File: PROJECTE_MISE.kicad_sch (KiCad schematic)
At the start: 46 parts, among them IC1 MSP430FR2355TPT, J1 conn_DFrobot, J10 SDA_{TP}, J11 SCL_{TP}, J12 SCL_{TP-GND}, J13 SPI_{TP-MISO}, J14 SPI_{TP-SS}, J15 SPI_{TP-SCLK}, J16 SPI_{TP-MOSI}, J17 SPI_{TP-GND}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

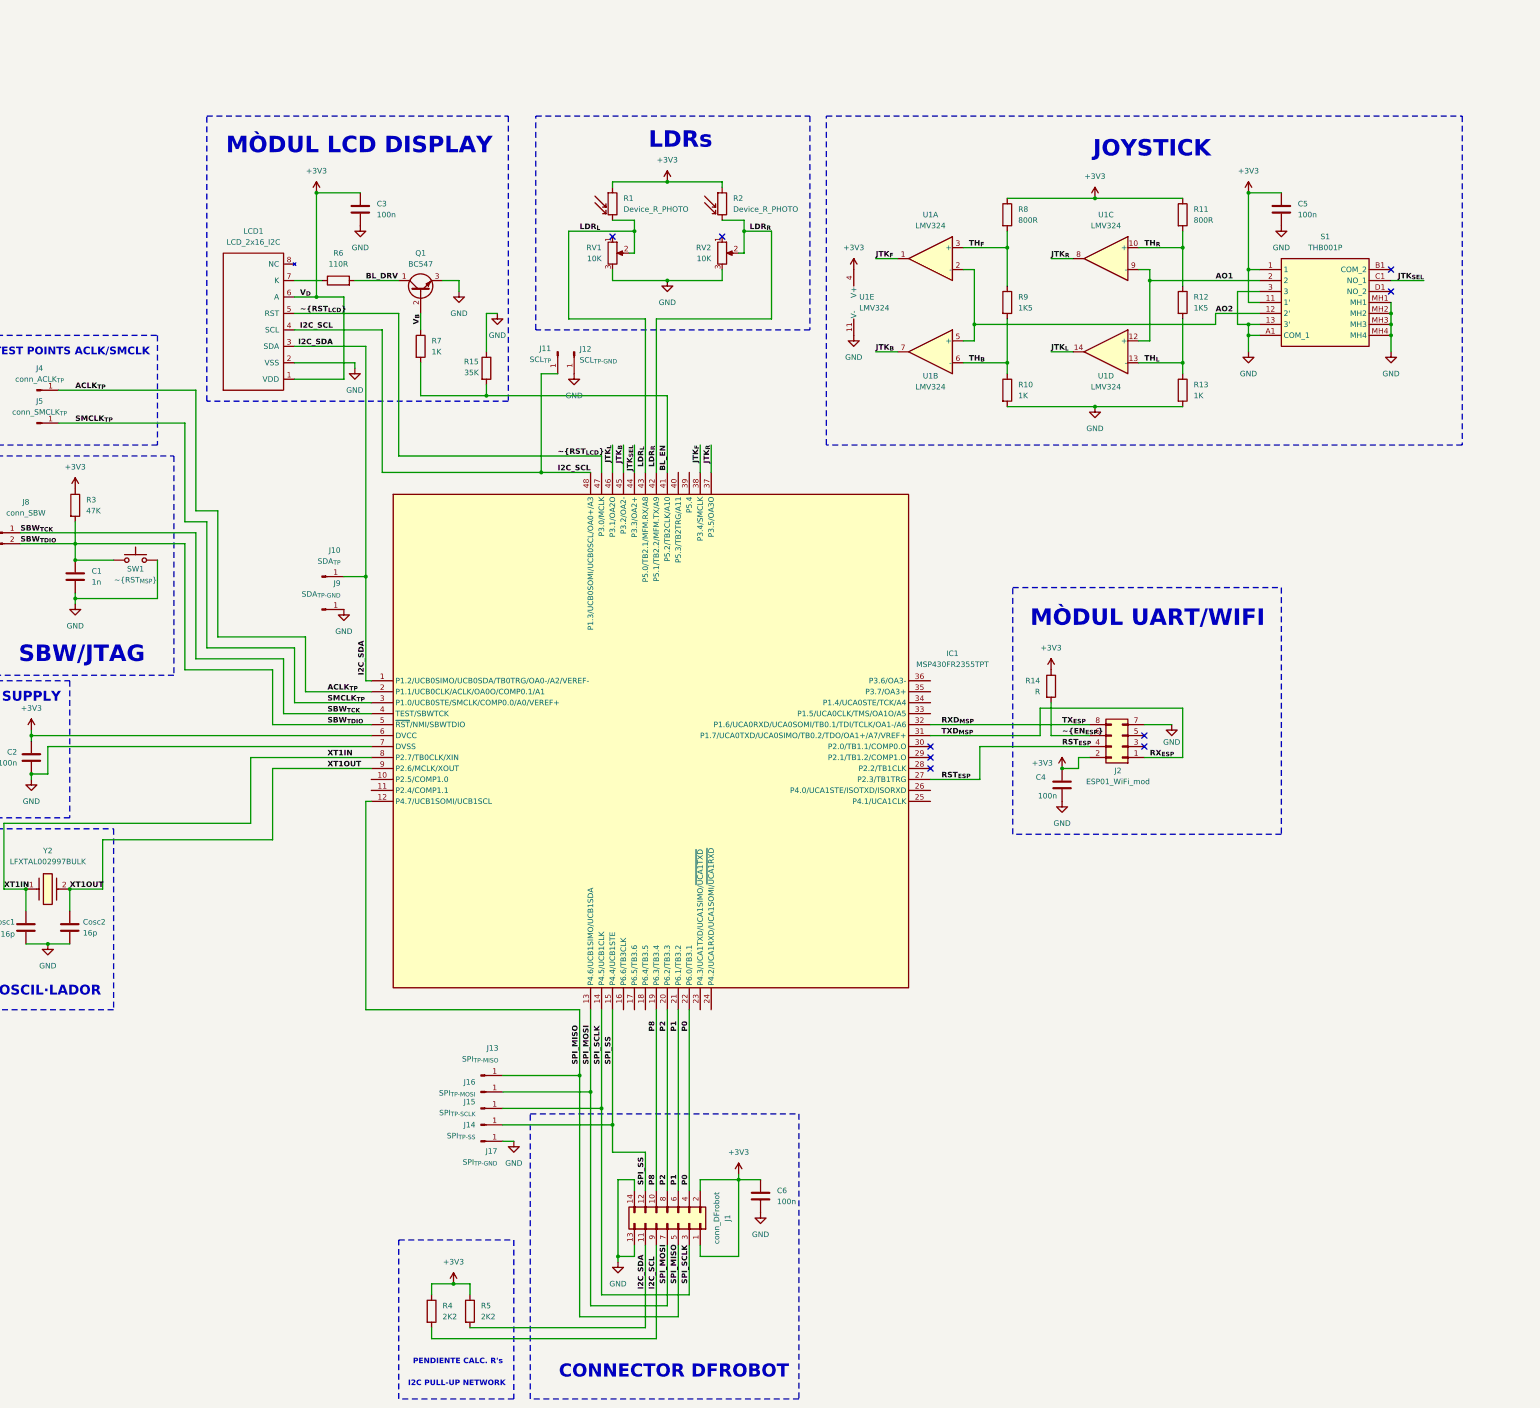
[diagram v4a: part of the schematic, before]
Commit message: placement i canvi esqu.
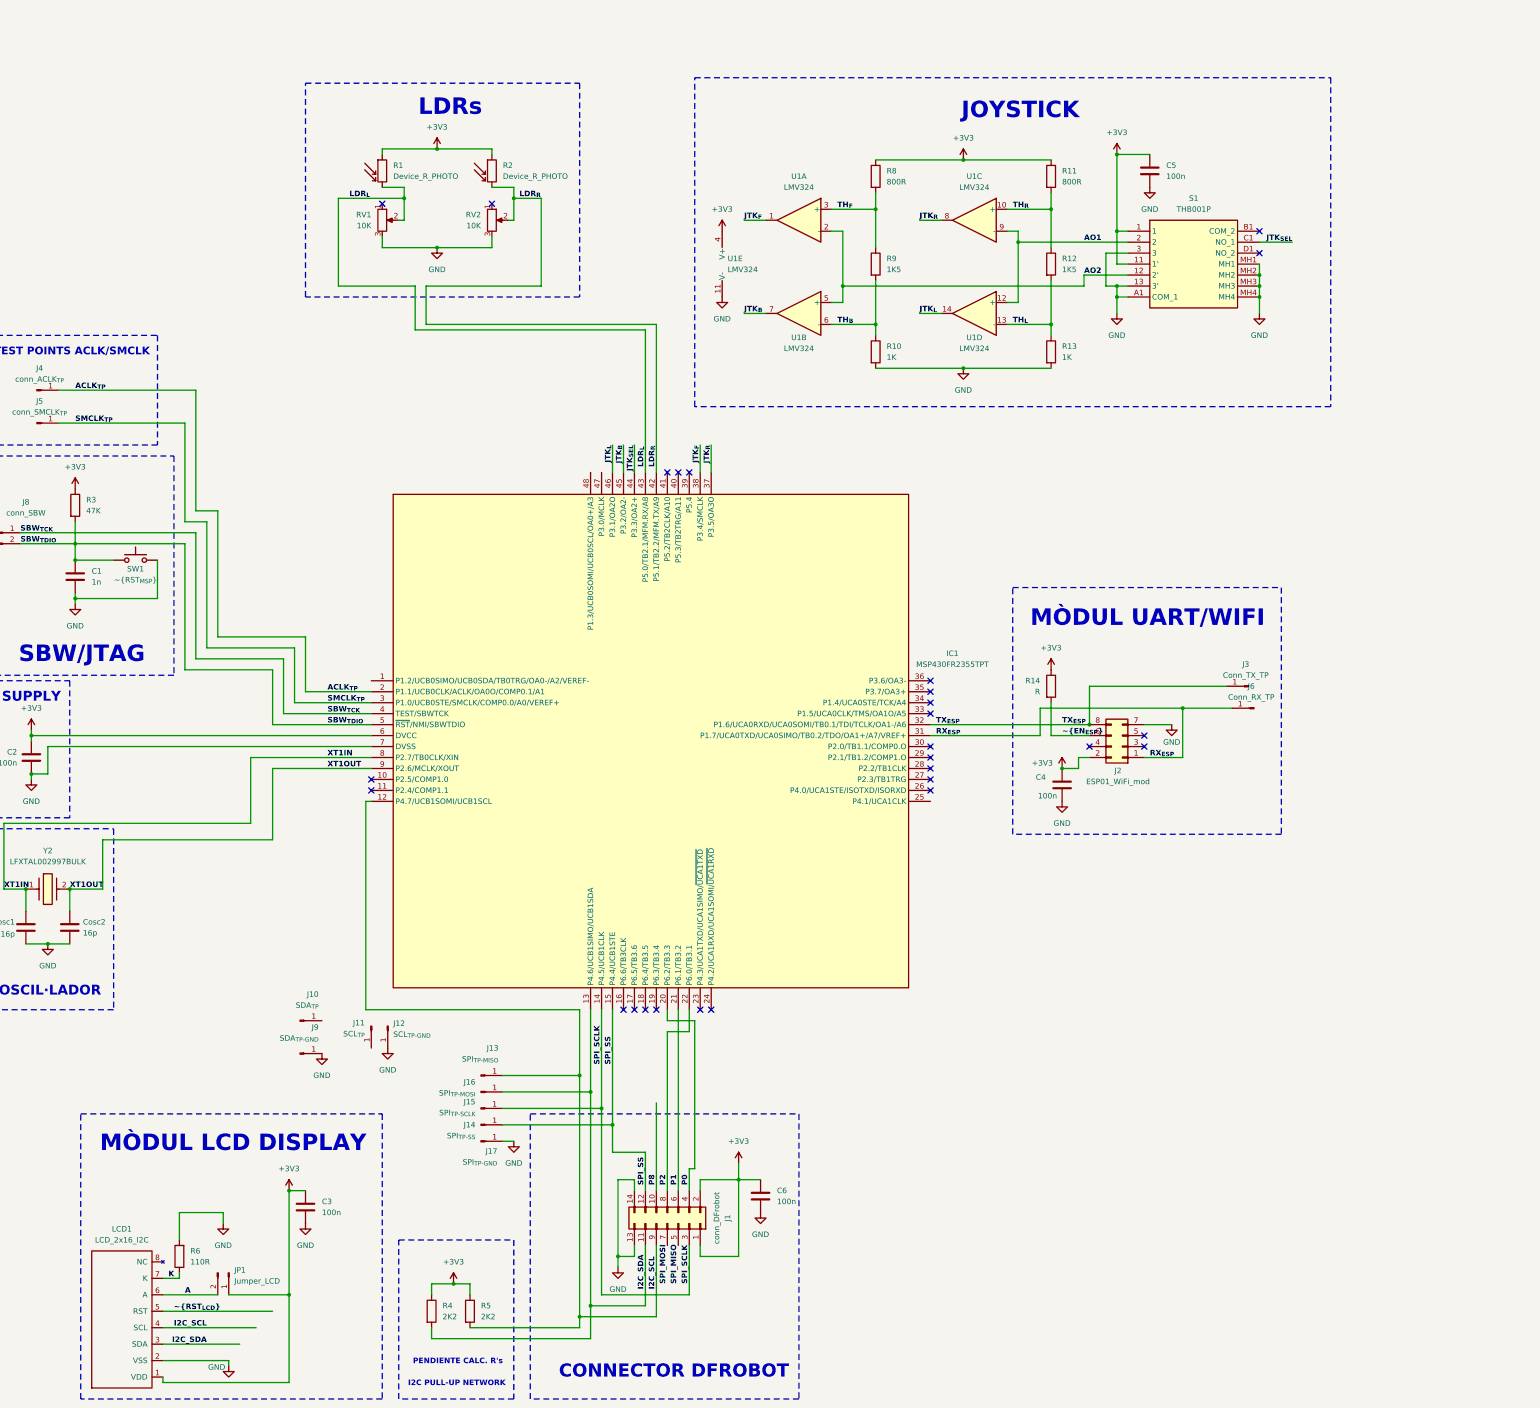
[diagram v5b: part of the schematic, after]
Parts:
- removed Q1: BC547, Package_TO_SOT_THT:TO-92_Inline, symbol Transistor_BJT:BC547
- removed R15: 35K, Resistor_SMD:R_0805_2012Metric, symbol Device:R
- removed R7: 1K, Resistor_SMD:R_0805_2012Metric, symbol Device:R
- added J3: Conn_TX_TP, Connector_PinHeader_1.00mm:PinHeader_1x01_P1.00mm_Vertical, symbol Connector:Conn_01x01_Pin
- added J6: Conn_RX_TP, Connector_PinHeader_1.00mm:PinHeader_1x01_P1.00mm_Vertical, symbol Connector:Conn_01x01_Pin
- added JP1: Jumper_LCD, Connector_PinHeader_1.00mm:PinHeader_1x02_P1.00mm_Vertical, symbol Connector:Conn_01x02_Pin
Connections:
- net BL_DRV is gone; now on net GND: R6.2
- net +3V3: now also JP1.1 (Pin_1); no longer LCD1.6 (A)
- net I2C_SCL: now also IC1.12 (P4.7/UCB1SOMI/UCB1SCL), J13.1 (Pin_1), R5.2; no longer IC1.48 (P1.3/UCB0SOMI/UCB0SCL/OA0+/A3), J11.1 (Pin_1), R4.2
- net I2C_SDA: now also IC1.13 (P4.6/UCB1SIMO/UCB1SDA), J16.1 (Pin_1), R4.2; no longer IC1.1 (P1.2/UCB0SIMO/UCB0SDA/TB0TRG/OA0-/A2/VEREF-), J10.1 (Pin_1), R5.2
- net P0: now also IC1.20 (P6.2/TB3.3); no longer IC1.22 (P6.0/TB3.1)
- net P2: now also IC1.22 (P6.0/TB3.1); no longer IC1.20 (P6.2/TB3.3)
- net P8: no longer IC1.19 (P6.3/TB3.4)
- net RX_{ESP}: now also J6.1 (Pin_1)
- net SPI_MISO: no longer IC1.12 (P4.7/UCB1SOMI/UCB1SCL), J1.5 (Pin_5), J13.1 (Pin_1)
- net SPI_MOSI: no longer IC1.13 (P4.6/UCB1SIMO/UCB1SDA), J1.7 (Pin_7), J16.1 (Pin_1)
- net ~{RST_{LCD}}: no longer IC1.47 (P3.0/MCLK)
- net K: now reaches LCD1.7 (K), R6.1
- net BL_EN: no longer names the net of IC1.41 (P5.2/TB2CLK/A10)
- net RST_{ESP}: no longer names the net of J2.4 (Pin_4)
- net RST_{ESP}: no longer IC1.27 (P2.3/TB1TRG)
- net RXD_{MSP} renamed TX_{ESP}
- net TX_{ESP}: now also J3.1 (Pin_1)
- new net A: JP1.2 (Pin_2), LCD1.6 (A)
- no-connect marks 9 -> 27
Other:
- moved on the sheet: C3, C5, J10, J11, J12, J9, LCD1, R1, R10, R11, R12, R13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

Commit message: acabat
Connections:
- net I2C_SCL: now also J11.1 (Pin_1); no longer J13.1 (Pin_1)
- net I2C_SDA: now also J10.1 (Pin_1); no longer J16.1 (Pin_1)
- net P8: now also IC1.27 (P2.3/TB1TRG)
- net SPI_MISO: now also IC1.24 (P4.2/UCA1RXD/UCA1SOMI/~{UCA1RXD}), J1.5 (Pin_5), J13.1 (Pin_1)
- net SPI_MOSI: now also IC1.23 (P4.3/UCA1TXD/UCA1SIMO/~{UCA1TXD}), J1.7 (Pin_7), J16.1 (Pin_1)
- net SPI_SCLK: now also IC1.25 (P4.1/UCA1CLK); no longer IC1.14 (P4.5/UCB1CLK)
- net SPI_SS: now also IC1.26 (P4.0/UCA1STE/ISOTXD/ISORXD); no longer IC1.15 (P4.4/UCB1STE)
- no-connect marks 27 -> 28
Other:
- moved on the sheet: J10, J11, J12, J13, J14, J15, J16, J17, J9
